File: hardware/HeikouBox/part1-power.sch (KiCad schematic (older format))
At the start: 15 parts, among them J101 5V, U101 LD1117S33TR, U102 LD1117S25TR, U103 LD1117S12TR

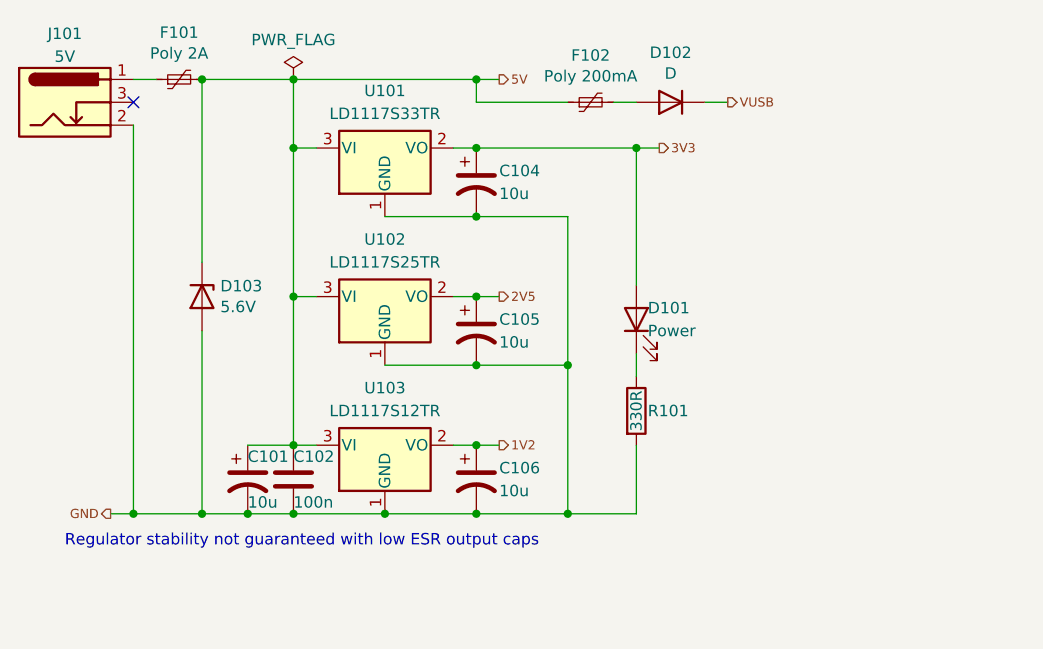
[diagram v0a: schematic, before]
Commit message: Run 1.2v vreg from 3.3v to spread power
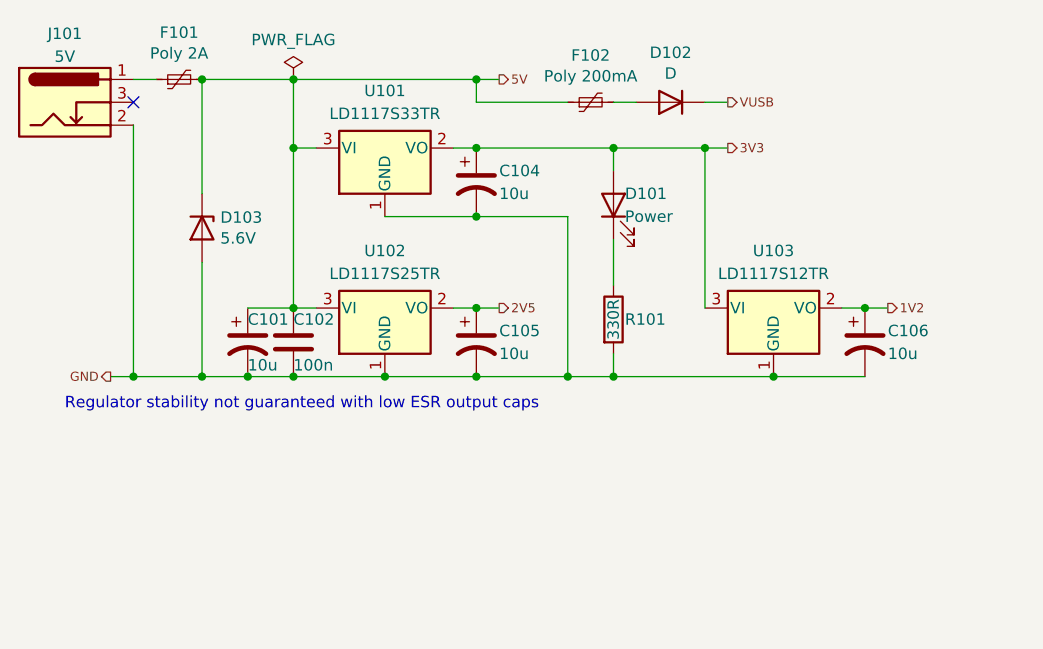
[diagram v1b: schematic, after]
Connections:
- net 3V3: now also U103.3 (VI)
- net 5V: no longer U103.3 (VI)
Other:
- moved on the sheet: C101, C102, C105, C106, D101, D103, R101, U102, U103

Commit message: Add 1ohm series resistors to regulator output caps
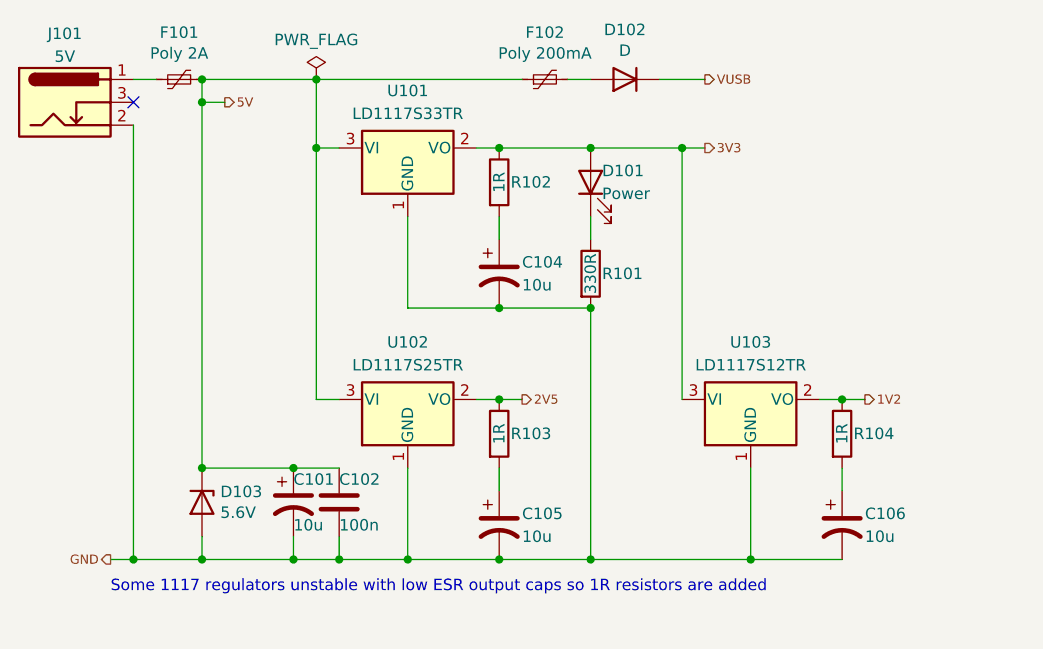
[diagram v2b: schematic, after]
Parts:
- added R102, R103, R104: 1R, Resistor_SMD:R_0805_2012Metric_Pad1.20x1.40mm_HandSolder, symbol Device:R
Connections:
- net 1V2: now also R104.1; no longer C106.1
- net 2V5: now also R103.1; no longer C105.1
- net 3V3: now also R102.1; no longer C104.1
- new net: C105.1, R103.2
- new net: C106.1, R104.2
- new net: C104.1, R102.2
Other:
- note added: "Some 1117 regulators unstable with low ESR output caps so 1R resistors are added"
- note removed: "Regulator stability not guaranteed with low ESR output caps"
- moved on the sheet: C101, C102, C104, C105, C106, D101, D102, D103, F102, R101, U101, U102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

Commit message: Cleanup, add regulator input caps
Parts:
- added C103, C107: 100n, Capacitor_SMD:C_0603_1608Metric_Pad1.08x0.95mm_HandSolder, symbol Device:C
- C101, C104, C105, C106: symbol Device:CP1 -> Device:C
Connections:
- net 3V3: now also C107.1
- net 5V: now also C103.1
- net GND: now also C103.2, C107.2
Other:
- note added: "Some 1117 regulators unstable with low ESR output caps so 1R resistors are added.\n5.6v zener for input overvoltage protection only, not strictly necessary."
- note removed: "Some 1117 regulators unstable with low ESR output caps so 1R resistors are added"
- moved on the sheet: C102, D101, D102, D103, F102, R101, R102, R103, R104, U101, U102, U103

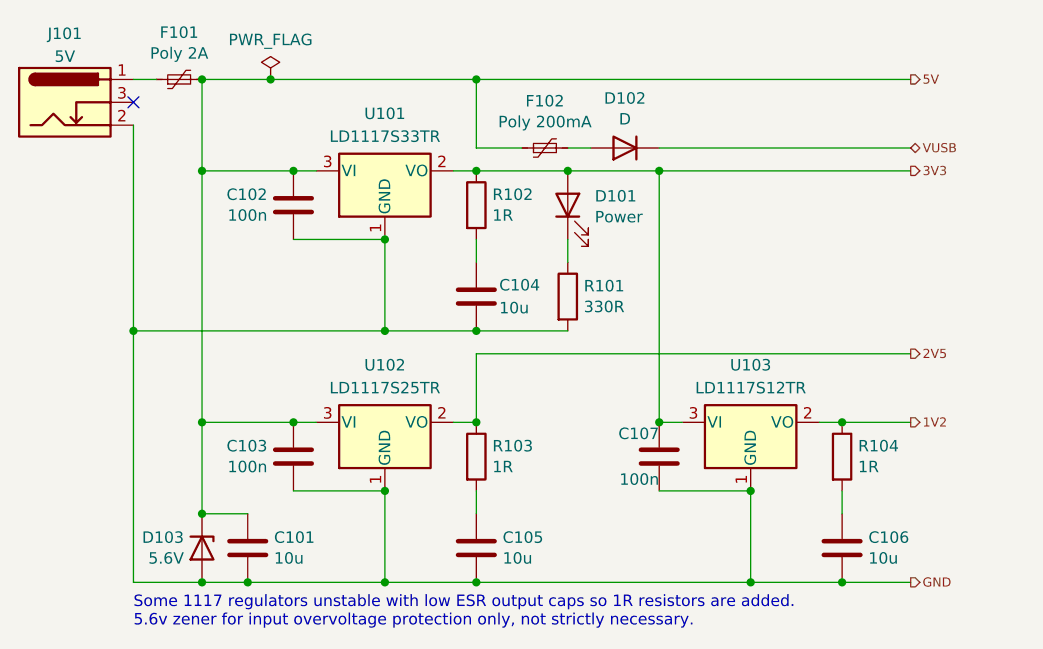
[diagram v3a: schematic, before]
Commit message: Cleanup, add rounded corners, bigger diode
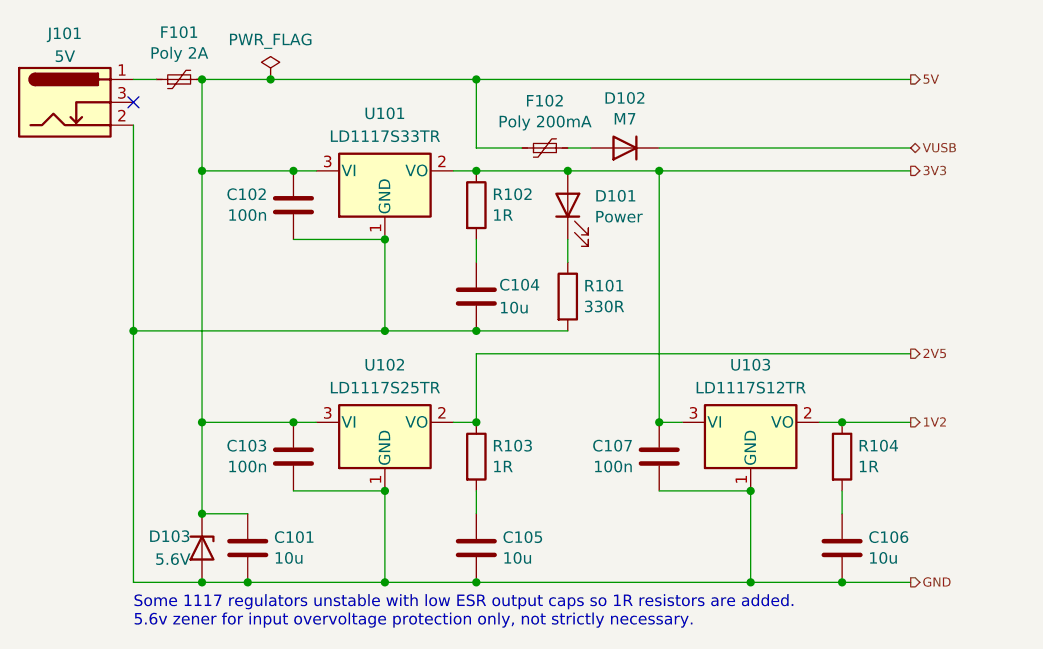
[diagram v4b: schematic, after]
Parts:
- D102: value D -> M7; footprint Diode_SMD:D_SOD-123 -> Diode_SMD:D_SMA
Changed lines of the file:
@@
 P 3250 1100
 F 0 "D102" H 3250 883 50  0000 C CNN
-F 1 "D" H 3250 974 50  0000 C CNN
-F 2 "Diode_SMD:D_SOD-123" H 3250 1100 50  0001 C CNN
+F 1 "M7" H 3250 974 50  0000 C CNN
+F 2 "Diode_SMD:D_SMA" H 3250 1100 50  0001 C CNN
 F 3 "~" H 3250 1100 50  0001 C CNN
 	1    3250 1100
@@
 AR Path="/644CBAED/63917676" Ref="C107"  Part="1"
 AR Path="/729F86A7/63917676" Ref="C?"  Part="1"
-F 0 "C107" H 3400 2550 50  0000 R CNN
-F 1 "100n" H 3400 2350 50  0000 R CNN
+F 0 "C107" H 3286 2496 50  0000 R CNN
+F 1 "100n" H 3286 2405 50  0000 R CNN
 F 2 "Capacitor_SMD:C_0603_1608Metric_Pad1.08x0.95mm_HandSolder" H 3438 2300 50  0001 C CNN
 F 3 "~" H 3400 2450 50  0001 C CNN
@@
 	1    0    0    -1
 $EndComp
+Wire Wire Line
+	2600 3000 3800 3000
+Wire Wire Line
+	2200 1900 1100 1900
+Connection ~ 2200 1900
+Connection ~ 1100 1900
+Wire Wire Line
+	1100 1900 1100 3000
 $Comp
 L Device:D_Zener D103
 U 1 1 644C5C9C
 P 1400 2850
-F 0 "D103" V 1354 2771 50  0000 R CNN
-F 1 "5.6V" V 1445 2771 50  0000 R CNN
+F 0 "D103" V 1350 2800 50  0000 R CNN
+F 1 "5.6V" V 1450 2800 50  0000 R CNN
 F 2 "Diode_SMD:D_SOD-123" H 1400 2850 50  0001 C CNN
 F 3 "~" H 1400 2850 50  0001 C CNN
@@
 	0    1    1    0
 $EndComp
-Wire Wire Line
-	2600 3000 3800 3000
-Wire Wire Line
-	2200 1900 1100 1900
-Connection ~ 2200 1900
-Connection ~ 1100 1900
-Wire Wire Line
-	1100 1900 1100 3000
 $EndSCHEMATC

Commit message: More tidy up, move vias
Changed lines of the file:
@@
 AR Path="/644CBAED/638456AF" Ref="R104"  Part="1"
 AR Path="/729F86A7/638456AF" Ref="R?"  Part="1"
-F 0 "R104" H 4270 2496 50  0000 L CNN
-F 1 "1R" H 4270 2405 50  0000 L CNN
+F 0 "R104" H 4250 2450 50  0000 L CNN
+F 1 "1R" V 4200 2450 50  0000 C CNN
 F 2 "Resistor_SMD:R_0805_2012Metric_Pad1.20x1.40mm_HandSolder" V 4130 2450 50  0001 C CNN
 F 3 "~" H 4200 2450 50  0001 C CNN
@@
 AR Path="/644CBAED/63836B0F" Ref="R103"  Part="1"
 AR Path="/729F86A7/63836B0F" Ref="R?"  Part="1"
-F 0 "R103" H 2670 2496 50  0000 L CNN
-F 1 "1R" H 2670 2405 50  0000 L CNN
+F 0 "R103" H 2650 2450 50  0000 L CNN
+F 1 "1R" V 2600 2450 50  0000 C CNN
 F 2 "Resistor_SMD:R_0805_2012Metric_Pad1.20x1.40mm_HandSolder" V 2530 2450 50  0001 C CNN
 F 3 "~" H 2600 2450 50  0001 C CNN
@@
 AR Path="/644CBAED/67C00DA5" Ref="R101"  Part="1"
 AR Path="/729F86A7/67C00DA5" Ref="R?"  Part="1"
-F 0 "R101" H 3070 1796 50  0000 L CNN
-F 1 "330R" H 3070 1705 50  0000 L CNN
+F 0 "R101" H 3050 1750 50  0000 L CNN
+F 1 "330R" V 3000 1750 50  0000 C CNN
 F 2 "Resistor_SMD:R_0603_1608Metric_Pad0.98x0.95mm_HandSolder" V 2930 1750 50  0001 C CNN
 F 3 "~" H 3000 1750 50  0001 C CNN
@@
 AR Path="/644CBAED/63867DB9" Ref="R102"  Part="1"
 AR Path="/729F86A7/63867DB9" Ref="R?"  Part="1"
-F 0 "R102" H 2670 1396 50  0000 L CNN
-F 1 "1R" H 2670 1305 50  0000 L CNN
+F 0 "R102" H 2650 1350 50  0000 L CNN
+F 1 "1R" V 2600 1350 50  0000 C CNN
 F 2 "Resistor_SMD:R_0805_2012Metric_Pad1.20x1.40mm_HandSolder" V 2530 1350 50  0001 C CNN
 F 3 "~" H 2600 1350 50  0001 C CNN

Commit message: I'm da giant cap that takes all of the space (smaller caps)
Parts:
- C101, C104, C105, C106: footprint Capacitor_SMD:C_1206_3216Metric_Pad1.33x1.80mm_HandSolder -> Capacitor_SMD:C_0805_2012Metric_Pad1.18x1.45mm_HandSolder
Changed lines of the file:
@@
 $Descr A4 11693 8268
 encoding utf-8
-Sheet 6 6
+Sheet 5 6
 Title "HeikouBox Mainboard - Power Suppli"
 Date "2022-11-11"
@@
 F 0 "C106" H 4315 2896 50  0000 L CNN
 F 1 "10u" H 4315 2805 50  0000 L CNN
-F 2 "Capacitor_SMD:C_1206_3216Metric_Pad1.33x1.80mm_HandSolder" H 4238 2700 50  0001 C CNN
+F 2 "Capacitor_SMD:C_0805_2012Metric_Pad1.18x1.45mm_HandSolder" H 4238 2700 50  0001 C CNN
 F 3 "~" H 4200 2850 50  0001 C CNN
 	1    4200 2850
@@
 F 0 "C105" H 2715 2896 50  0000 L CNN
 F 1 "10u" H 2715 2805 50  0000 L CNN
-F 2 "Capacitor_SMD:C_1206_3216Metric_Pad1.33x1.80mm_HandSolder" H 2638 2700 50  0001 C CNN
+F 2 "Capacitor_SMD:C_0805_2012Metric_Pad1.18x1.45mm_HandSolder" H 2638 2700 50  0001 C CNN
 F 3 "~" H 2600 2850 50  0001 C CNN
 	1    2600 2850
@@
 F 0 "C104" H 2700 1800 50  0000 L CNN
 F 1 "10u" H 2700 1700 50  0000 L CNN
-F 2 "Capacitor_SMD:C_1206_3216Metric_Pad1.33x1.80mm_HandSolder" H 2638 1600 50  0001 C CNN
+F 2 "Capacitor_SMD:C_0805_2012Metric_Pad1.18x1.45mm_HandSolder" H 2638 1600 50  0001 C CNN
 F 3 "~" H 2600 1750 50  0001 C CNN
 	1    2600 1750
@@
 F 0 "C101" H 1715 2896 50  0000 L CNN
 F 1 "10u" H 1715 2805 50  0000 L CNN
-F 2 "Capacitor_SMD:C_1206_3216Metric_Pad1.33x1.80mm_HandSolder" H 1638 2700 50  0001 C CNN
+F 2 "Capacitor_SMD:C_0805_2012Metric_Pad1.18x1.45mm_HandSolder" H 1638 2700 50  0001 C CNN
 F 3 "~" H 1600 2850 50  0001 C CNN
 	1    1600 2850

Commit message: BOM reduction
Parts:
- R101: value 330R -> 1K
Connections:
- net 3V3: now also R101.1; no longer D101.2 (A)
- net GND: now also D101.1 (K); no longer R101.2
- new net: D101.2 (A), R101.2
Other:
- moved on the sheet: C101, D101, D103, R101
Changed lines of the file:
@@
 	0    -1   -1   0
 $EndComp
-Text HLabel 4500 1200 2    40   Output ~ 0
-3V3
 Wire Wire Line
 	1100 800  1200 800
@@
 Wire Wire Line
 	2200 2600 2200 3000
-Connection ~ 1400 3000
-Wire Wire Line
-	1100 3000 1400 3000
 Wire Wire Line
 	4500 3000 4200 3000
@@
 L Device:LED D?
 U 1 1 67C00D9C
-P 3000 1350
+P 3000 1750
 AR Path="/67C00D9C" Ref="D?"  Part="1"
 AR Path="/644CBAED/67C00D9C" Ref="D101"  Part="1"
 AR Path="/729F86A7/67C00D9C" Ref="D?"  Part="1"
-F 0 "D101" V 3039 1232 50  0000 R CNN
-F 1 "Power" V 2948 1232 50  0000 R CNN
-F 2 "LED_SMD:LED_0603_1608Metric_Pad1.05x0.95mm_HandSolder" H 3000 1350 50  0001 C CNN
-F 3 "~" H 3000 1350 50  0001 C CNN
-	1    3000 1350
+F 0 "D101" V 3039 1632 50  0000 R CNN
+F 1 "Power" V 2948 1632 50  0000 R CNN
+F 2 "LED_SMD:LED_0603_1608Metric_Pad1.05x0.95mm_HandSolder" H 3000 1750 50  0001 C CNN
+F 3 "~" H 3000 1750 50  0001 C CNN
+	1    3000 1750
 	0    -1   -1   0
 $EndComp
@@
 L Device:R R?
 U 1 1 67C00DA5
-P 3000 1750
+P 3000 1350
 AR Path="/67C00DA5" Ref="R?"  Part="1"
 AR Path="/644CBAED/67C00DA5" Ref="R101"  Part="1"
 AR Path="/729F86A7/67C00DA5" Ref="R?"  Part="1"
-F 0 "R101" H 3050 1750 50  0000 L CNN
-F 1 "330R" V 3000 1750 50  0000 C CNN
-F 2 "Resistor_SMD:R_0603_1608Metric_Pad0.98x0.95mm_HandSolder" V 2930 1750 50  0001 C CNN
-F 3 "~" H 3000 1750 50  0001 C CNN
-	1    3000 1750
+F 0 "R101" H 3050 1350 50  0000 L CNN
+F 1 "1K" V 3000 1350 50  0000 C CNN
+F 2 "Resistor_SMD:R_0603_1608Metric_Pad0.98x0.95mm_HandSolder" V 2930 1350 50  0001 C CNN
+F 3 "~" H 3000 1350 50  0001 C CNN
+	1    3000 1350
 	1    0    0    -1
 $EndComp
@@
 	1    0    0    -1
 $EndComp
-Connection ~ 1400 2700
 Connection ~ 1800 2300
 Wire Wire Line
@@
 	3400 2600 3800 2600
 Connection ~ 3800 2600
-Wire Wire Line
-	3400 2300 3400 1200
 Connection ~ 3400 2300
-Connection ~ 3400 1200
-Wire Wire Line
-	3400 1200 4500 1200
 Connection ~ 4200 3000
 Wire Wire Line
@@
 Wire Wire Line
 	1600 3000 2200 3000
+Connection ~ 1600 3000
+Wire Wire Line
+	1600 2700 1400 2700
+Wire Wire Line
+	2600 3000 3800 3000
+Wire Wire Line
+	2200 1900 1100 1900
+Connection ~ 2200 1900
+Connection ~ 1100 1900
+Wire Wire Line
+	1100 1900 1100 3000
+$Comp
+L Device:D_Zener D103
+U 1 1 644C5C9C
+P 1600 2850
+F 0 "D103" V 1550 2950 50  0000 L CNN
+F 1 "5.6V" V 1650 2950 50  0000 L CNN
+F 2 "Diode_SMD:D_SOD-123" H 1600 2850 50  0001 C CNN
+F 3 "~" H 1600 2850 50  0001 C CNN
+	1    1600 2850
+	0    1    1    0
+$EndComp
+Wire Wire Line
+	1100 3000 1400 3000
+Connection ~ 1400 2700
+Connection ~ 1400 3000
 Wire Wire Line
 	1400 3000 1600 3000
-Connection ~ 1600 3000
-Wire Wire Line
-	1600 2700 1400 2700
 $Comp
 L Device:C C?
 U 1 1 67C00DB6
-P 1600 2850
+P 1400 2850
 AR Path="/67C00DB6" Ref="C?"  Part="1"
 AR Path="/644CBAED/67C00DB6" Ref="C101"  Part="1"
 AR Path="/729F86A7/67C00DB6" Ref="C?"  Part="1"
-F 0 "C101" H 1715 2896 50  0000 L CNN
-F 1 "10u" H 1715 2805 50  0000 L CNN
-F 2 "Capacitor_SMD:C_0805_2012Metric_Pad1.18x1.45mm_HandSolder" H 1638 2700 50  0001 C CNN
-F 3 "~" H 1600 2850 50  0001 C CNN
-	1    1600 2850
-	1    0    0    -1
-$EndComp
-Wire Wire Line
-	2600 3000 3800 3000
-Wire Wire Line
-	2200 1900 1100 1900
-Connection ~ 2200 1900
-Connection ~ 1100 1900
-Wire Wire Line
-	1100 1900 1100 3000
-$Comp
-L Device:D_Zener D103
-U 1 1 644C5C9C
-P 1400 2850
-F 0 "D103" V 1350 2800 50  0000 R CNN
-F 1 "5.6V" V 1450 2800 50  0000 R CNN
-F 2 "Diode_SMD:D_SOD-123" H 1400 2850 50  0001 C CNN
+F 0 "C101" H 1300 2900 50  0000 R CNN
+F 1 "10u" H 1300 2800 50  0000 R CNN
+F 2 "Capacitor_SMD:C_0805_2012Metric_Pad1.18x1.45mm_HandSolder" H 1438 2700 50  0001 C CNN
 F 3 "~" H 1400 2850 50  0001 C CNN
 	1    1400 2850
-	0    1    1    0
-$EndComp
+	1    0    0    -1
+$EndComp
+Wire Wire Line
+	3400 2300 3400 1500
+Wire Wire Line
+	3400 1500 4500 1500
+Text HLabel 4500 1500 2    40   Output ~ 0
+3V3
+Connection ~ 3400 1500
+Wire Wire Line
+	3400 1500 3400 1200
 $EndSCHEMATC
